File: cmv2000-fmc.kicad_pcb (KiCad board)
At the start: 4 copper layers, 70 x 35 mm, 5 parts, among them P1 FMC_LPC, P2 CONN_31, P3 CONN_51, P4 CONN_2

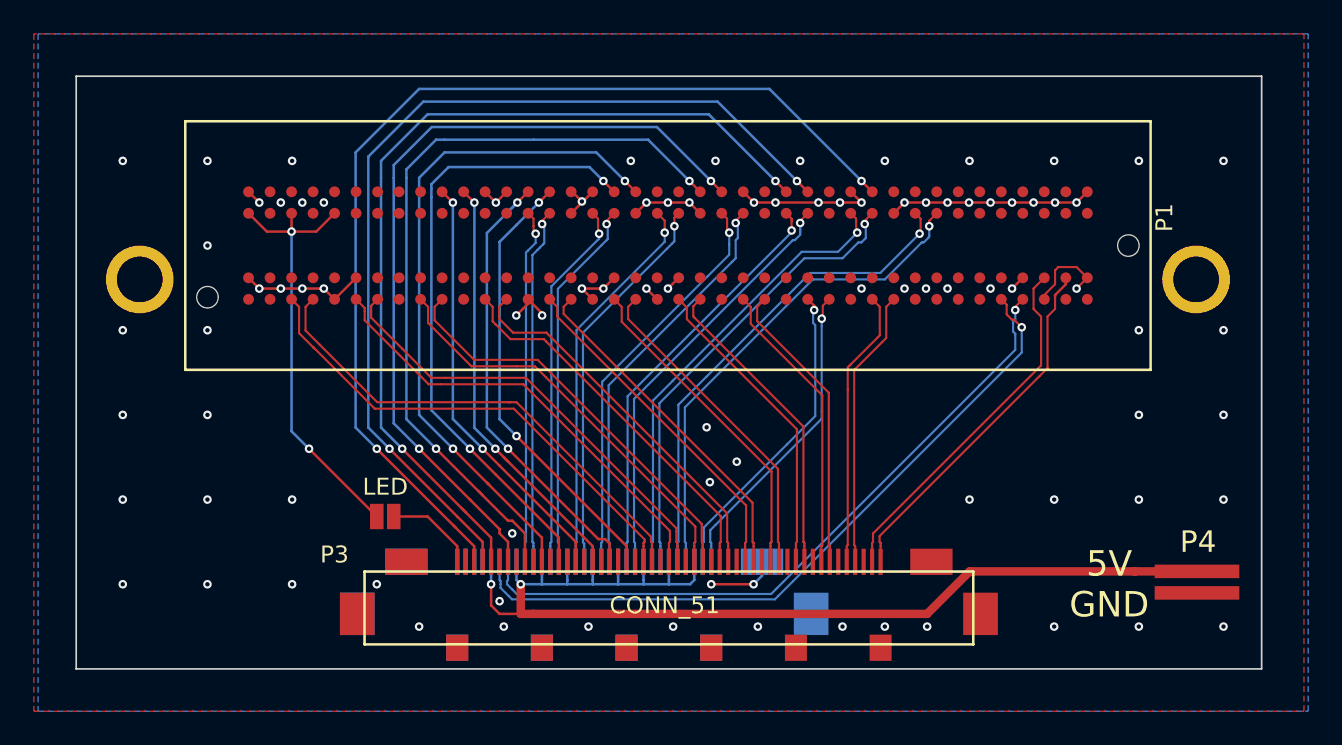
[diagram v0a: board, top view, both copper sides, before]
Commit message: fix mirrored JAE connectors (P2 and P3), correct signal names
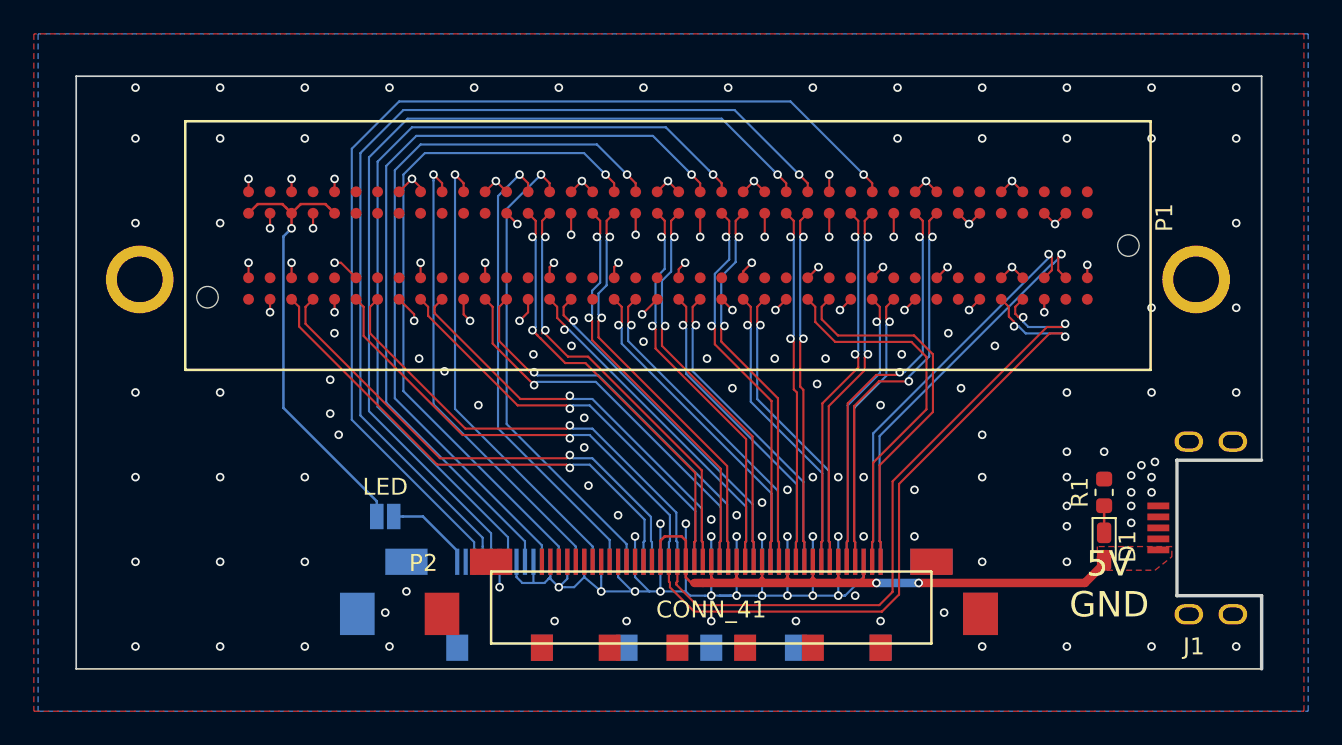
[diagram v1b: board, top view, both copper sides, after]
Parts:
- removed P4: CONN_2, owncomp:FLATCONN_2
- added D1: LED, LED_SMD:LED_0603_1608Metric_Castellated, F.Cu at (173.2, 112.8)
- added J1: USB_B_Micro, owncomp:JAE-USB-DX4R005JJ7, F.Cu at (182.5, 111.7)
- added R1: R, Resistor_SMD:R_0603_1608Metric, F.Cu at (173.2, 109.6)
- JP1, P3: moved to B.Cu
- P2: value CONN_31 -> CONN_41; footprint owncomp:FI-RE31S-HF-R1500 -> owncomp:FI-RE41S-HF-R1500; moved to F.Cu
- moved P2 7.50 mm to (150.0, 114.2), turned to 0 degrees
- turned P3 to 180 degrees
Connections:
- P1 pad C02: Net-(P1-PadC02) -> (no net)
- P1 pad C03: Net-(P1-PadC03) -> (no net)
- P1 pad C06: Net-(P1-PadC06) -> (no net)
- P1 pad C07: Net-(P1-PadC07) -> (no net)
- P1 pad C10: Net-(P1-PadC10) -> (no net)
- P1 pad C11: /SYS_RES_N -> /SDA
- P1 pad C14: /SPI_EN -> /SCL
- P1 pad C15: /SPI_CLK -> /SYS_RES_N
- P1 pad C18: /T_EXP1 -> /SPI_CLK
- P1 pad C19: /SPI_OUT -> /SPI_EN
- P1 pad C22: /SPI_IN -> /SPI_OUT
- P1 pad C23: /T_EXP2 -> /SPI_IN
- P1 pad C30: /SCL -> /T_EXP2
- P1 pad C31: /SDA -> /T_EXP1
- P1 pad C34: Net-(P1-PadC34) -> (no net)
- P1 pad C35: Net-(P1-PadC35) -> (no net)
- P1 pad C37: Net-(P1-PadC37) -> (no net)
- P1 pad C39: Net-(P1-PadC39) -> (no net)
- P1 pad D01: Net-(P1-PadD01) -> (no net)
- P1 pad D04: Net-(P1-PadD04) -> (no net)
- P1 pad D05: Net-(P1-PadD05) -> (no net)
- P1 pad D08: /LVDS_CTR_P -> /LVDS_16_P
- P1 pad D09: /LVDS_CTR_N -> /LVDS_16_N
- P1 pad D11: /LVDS_2_P -> /LVDS_14_P
- P1 pad D12: /LVDS_2_N -> /LVDS_14_N
- P1 pad D14: /LVDS_4_P -> /LVDS_12_P
- P1 pad D15: /LVDS_4_N -> /LVDS_12_N
- P1 pad D17: /LVDS_5_P -> /LVDS_11_P
- P1 pad D18: /LVDS_5_N -> /LVDS_11_N
- P1 pad D20: /LVDS_7_P -> /LVDS_6_P
- P1 pad D21: /LVDS_7_N -> /LVDS_6_N
- P1 pad D23: /LVDS_11_P -> /LVDS_5_P
- P1 pad D24: /LVDS_11_N -> /LVDS_5_N
- P1 pad D26: /LVDS_13_P -> /LVDS_1_P
- P1 pad D27: /LVDS_13_N -> /LVDS_1_N
- P1 pad D29: Net-(P1-PadD29) -> (no net)
- P1 pad D30: Net-(P1-PadD30) -> (no net)
- P1 pad D31: Net-(P1-PadD31) -> (no net)
- P1 pad D32: Net-(P1-PadD32) -> (no net)
- P1 pad D33: Net-(P1-PadD33) -> (no net)
- P1 pad D34: Net-(P1-PadD34) -> (no net)
- P1 pad D35: Net-(P1-PadD35) -> (no net)
- P1 pad G06: Net-(P1-PadG06) -> (no net)
- P1 pad G07: Net-(P1-PadG07) -> (no net)
- P1 pad G09: Net-(P1-PadG09) -> (no net)
- P1 pad G10: Net-(P1-PadG10) -> (no net)
- P1 pad G12: Net-(P1-PadG12) -> (no net)
- P1 pad G13: Net-(P1-PadG13) -> (no net)
- P1 pad G15: Net-(P1-PadG15) -> (no net)
- P1 pad G16: Net-(P1-PadG16) -> (no net)
- P1 pad G18: Net-(P1-PadG18) -> (no net)
- P1 pad G19: Net-(P1-PadG19) -> (no net)
- P1 pad G21: Net-(P1-PadG21) -> (no net)
- P1 pad G22: Net-(P1-PadG22) -> (no net)
- P1 pad G24: Net-(P1-PadG24) -> (no net)
- P1 pad G25: Net-(P1-PadG25) -> (no net)
- P1 pad G27: Net-(P1-PadG27) -> (no net)
- P1 pad G28: Net-(P1-PadG28) -> (no net)
- P1 pad G30: Net-(P1-PadG30) -> (no net)
- P1 pad G31: Net-(P1-PadG31) -> (no net)
- P1 pad G33: Net-(P1-PadG33) -> (no net)
- P1 pad G34: Net-(P1-PadG34) -> (no net)
- P1 pad G36: Net-(P1-PadG36) -> (no net)
- P1 pad G37: Net-(P1-PadG37) -> (no net)
- P1 pad G39: Net-(P1-PadG39) -> (no net)
- P1 pad H01: Net-(P1-PadH01) -> (no net)
- P1 pad H02: Net-(P1-PadH02) -> (no net)
- P1 pad H07: Net-(P1-PadH07) -> (no net)
- P1 pad H08: Net-(P1-PadH08) -> (no net)
- P1 pad H10: /LVDS_1_P -> /LVDS_13_P
- P1 pad H11: /LVDS_1_N -> /LVDS_13_N
- P1 pad H13: /LVDS_3_P -> /LVDS_15_P
- P1 pad H14: /LVDS_3_N -> /LVDS_15_N
- P1 pad H16: /LVDS_6_P -> /LVDS_10_P
- P1 pad H17: /LVDS_6_N -> /LVDS_10_N
- P1 pad H19: /LVDS_8_P -> /LVDS_7_P
- P1 pad H20: /LVDS_8_N -> /LVDS_7_N
- P1 pad H25: /LVDS_10_P -> /LVDS_8_P
- P1 pad H26: /LVDS_10_N -> /LVDS_8_N
- P1 pad H28: /LVDS_12_P -> /LVDS_3_P
- P1 pad H29: /LVDS_12_N -> /LVDS_3_N
- P1 pad H31: /LVDS_14_P -> /LVDS_4_P
- P1 pad H32: /LVDS_14_N -> /LVDS_4_N
- P1 pad H34: /LVDS_15_P -> /LVDS_2_P
- P1 pad H35: /LVDS_15_N -> /LVDS_2_N
- P1 pad H37: /LVDS_16_P -> /LVDS_CTR_P
- P1 pad H38: /LVDS_16_N -> /LVDS_CTR_N
- P1 pad H40: Net-(P1-PadH40) -> (no net)
- P2 pad 1: /LVDS_3_P -> (no net)
- P2 pad 10: /LVDS_4_P -> (no net)
- P2 pad 11: /LVDS_4_N -> (no net)
- P2 pad 12: /5V -> (no net)
- P2 pad 13: /LVDS_5_P -> (no net)
- P2 pad 14: /LVDS_5_N -> (no net)
- P2 pad 16: /LVDS_7_P -> /LVDS_CLK_IN_N
- P2 pad 17: /LVDS_7_N -> /LVDS_CLK_IN_P
- P2 pad 19: /LVDS_11_P -> /LVDS_1_N
- P2 pad 2: /LVDS_3_N -> (no net)
- P2 pad 20: /LVDS_11_N -> /LVDS_1_P
- P2 pad 22: /LVDS_13_P -> /LVDS_5_N
- P2 pad 23: /LVDS_13_N -> /LVDS_5_P
- P2 pad 25: /LVDS_CLK_IN_P -> /LVDS_6_N
- P2 pad 26: /LVDS_CLK_IN_N -> /LVDS_6_P
- P2 pad 28: Net-(P2-Pad28) -> /LVDS_11_N
- P2 pad 29: Net-(P2-Pad29) -> /LVDS_11_P
- P2 pad 3: /5V -> (no net)
- P2 pad 30: Net-(P2-Pad30) -> /5V
- P2 pad 31: Net-(P2-Pad31) -> /LVDS_12_N
- P2 pad 32: GND -> /LVDS_12_P
- P2 pad 33: GND -> /5V
- P2 pad 34: GND -> /LVDS_14_N
- P2 pad 35: GND -> /LVDS_14_P
- P2 pad 36: GND -> /5V
- P2 pad 37: GND -> /LVDS_16_N
- P2 pad 38: GND -> /LVDS_16_P
- P2 pad 39: GND -> /5V
- P2 pad 4: /LVDS_CTR_P -> (no net)
- P2 pad 5: /LVDS_CTR_N -> (no net)
- P2 pad 6: /5V -> (no net)
- P2 pad 7: /LVDS_2_P -> (no net)
- P2 pad 8: /LVDS_2_N -> (no net)
- P2 pad 9: /5V -> (no net)
- P3 pad 1: /LED -> /LVDS_CLK_OUT_P
- P3 pad 10: GND -> /LVDS_7_P
- P3 pad 11: /SPI_IN -> /LVDS_7_N
- P3 pad 13: /T_EXP2 -> /LVDS_9_P
- P3 pad 14: GND -> /LVDS_9_N
- P3 pad 15: /SDA -> GND
- P3 pad 16: GND -> /LVDS_8_P
- P3 pad 17: /SCL -> /LVDS_8_N
- P3 pad 19: /FRAME_REQ -> /LVDS_3_P
- P3 pad 2: /A0 -> /LVDS_CLK_OUT_N
- P3 pad 20: GND -> /LVDS_3_N
- P3 pad 21: /CLK_IN -> GND
- P3 pad 22: GND -> /LVDS_4_P
- P3 pad 23: /LVDS_16_N -> /LVDS_4_N
- P3 pad 24: /LVDS_16_P -> GND
- P3 pad 25: GND -> /LVDS_2_P
- P3 pad 26: /LVDS_15_N -> /LVDS_2_N
- P3 pad 27: /LVDS_15_P -> GND
- P3 pad 28: GND -> /LVDS_CTR_P
- P3 pad 29: /LVDS_14_N -> /LVDS_CTR_N
- P3 pad 3: /SYS_RES_N -> GND
- P3 pad 30: /LVDS_14_P -> GND
- P3 pad 31: GND -> /CLK_IN
- P3 pad 32: /LVDS_12_N -> GND
- P3 pad 33: /LVDS_12_P -> /FRAME_REQ
- P3 pad 35: /LVDS_10_N -> /T_EXP2
- P3 pad 36: /LVDS_10_P -> GND
- P3 pad 37: GND -> /T_EXP1
- P3 pad 38: /LVDS_9_N -> GND
- P3 pad 39: /LVDS_9_P -> /SPI_IN
- P3 pad 4: /SPI_EN -> /LVDS_13_P
- P3 pad 41: /LVDS_8_N -> /SPI_OUT
- P3 pad 42: /LVDS_8_P -> GND
- P3 pad 43: GND -> /SPI_EN
- P3 pad 44: /LVDS_6_N -> GND
- P3 pad 45: /LVDS_6_P -> /SPI_CLK
- P3 pad 47: /LVDS_1_N -> /SYS_RES_N
- P3 pad 48: /LVDS_1_P -> /SCL
- P3 pad 49: GND -> /SDA
- P3 pad 5: /SPI_CLK -> /LVDS_13_N
- P3 pad 50: /LVDS_CLK_OUT_N -> (no net)
- P3 pad 51: /LVDS_CLK_OUT_P -> /LED
- P3 pad 7: /T_EXP1 -> /LVDS_10_P
- P3 pad 8: GND -> /LVDS_10_N
- P3 pad 9: /SPI_OUT -> GND
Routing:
- net GND: track 332.5 -> 125.7 mm, vias 89 -> 173
- net /SDA: track 25.1 -> 61.8 mm, vias 2 -> 1
- net /SCL: track 25.4 -> 56.9 mm, vias 2 -> 1
- net /T_EXP1: track 48.2 -> 27.6 mm, vias 2 -> 1
- net /5V: track 68.1 -> 48.1 mm
- net /T_EXP2: track 37.2 -> 27.5 mm, vias 2 -> 1
- net /LVDS_1_P: track 16.5 -> 25.8 mm, vias 0 -> 2
- net /LVDS_1_N: track 16.7 -> 26.0 mm, vias 0 -> 2
- net /SPI_EN: track 56.2 -> 47.7 mm, vias 2 -> 1
- net /SYS_RES_N: track 61.8 -> 54.5 mm, vias 2 -> 1
- net /LVDS_6_N: track 17.5 -> 23.5 mm, vias 0 -> 2
- net /LVDS_6_P: track 17.5 -> 23.5 mm, vias 0 -> 2
- net /LVDS_16_N: track 29.1 -> 23.7 mm, vias 0 -> 2
- net /LVDS_16_P: track 29.2 -> 23.8 mm, vias 0 -> 2
- net /LVDS_3_P: track 18.7 -> 23.5 mm
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- added copper zone on F.Cu, net /5V
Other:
- outline, holes or cut-outs redrawn
- board text added: "CMV2000 to FMC v0.2 2018-12-03"
- board text removed: "CMV2000 to FMC v0.1 2014-12-09"

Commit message: first version of layout (still WIP)
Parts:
- added C1: 10uF, 25V, Capacitor_SMD:C_1206_3216Metric, B.Cu at (180.7, 111.2)
- added C10: TBD, Capacitor_SMD:C_0805_2012Metric, B.Cu at (166.5, 112.1)
- added C2: 100n, Capacitor_SMD:C_0402_1005Metric, B.Cu at (128.2, 96.2)
- added C3: 10n, Capacitor_SMD:C_0402_1005Metric, B.Cu at (177.5, 113.8)
- added C4: 22uF, 10V, Capacitor_SMD:C_1206_3216Metric, B.Cu at (174.1, 113.8)
- added C5: 100n, Capacitor_SMD:C_0402_1005Metric, B.Cu at (128.2, 92.0)
- added C6: 1u, Capacitor_SMD:C_0603_1608Metric, B.Cu at (179.0, 93.0)
- added C7: 100n, Capacitor_SMD:C_0402_1005Metric, B.Cu at (114.4, 89.4)
- added C8: 1n, Capacitor_SMD:C_0402_1005Metric, B.Cu at (178.6, 88.4)
- added C9: 100n, Capacitor_SMD:C_0402_1005Metric, B.Cu at (116.4, 94.0)
- added D2: LED, footprints:150060VS75000, B.Cu at (116.0, 87.0)
- added D3: LED, footprints:150060VS75000, B.Cu at (122.1, 115.3)
- added J10: LVDS_CTR_P, footprints:U.FL-R-SMT-1, B.Cu at (130.8, 106.6)
- added J11: LVDS_CTR_N, footprints:U.FL-R-SMT-1, B.Cu at (135.3, 106.6)
- added J12: LVDS_1_P, footprints:U.FL-R-SMT-1, B.Cu at (142.9, 92.0)
- added J13: LVDS_1_N, footprints:U.FL-R-SMT-1, B.Cu at (137.8, 92.0)
- added J14: LVDS_2_P, footprints:U.FL-R-SMT-1, B.Cu at (136.9, 97.3)
- added J15: LVDS_2_N, footprints:U.FL-R-SMT-1, B.Cu at (132.6, 97.4)
- added J2: Conn_02x05, footprints:TSM-105-01-L-DV, B.Cu at (120.8, 107.0)
- added J3: LVDS_CLK_IN_P, footprints:U.FL-R-SMT-1, B.Cu at (164.1, 102.8)
- added J4: LVDS_CLK_IN_N, footprints:U.FL-R-SMT-1, B.Cu at (172.1, 102.8)
- added J5: LVDS_CLK_OUT_P, footprints:U.FL-R-SMT-1, B.Cu at (172.6, 92.2)
- added J6: LVDS_CLK_OUT_N, footprints:U.FL-R-SMT-1, B.Cu at (168.1, 92.2)
- added J7: CLK_IN, footprints:U.FL-R-SMT-1, B.Cu at (130.4, 101.2)
- added J8: CLK_IN, footprints:U.FL-R-SMT-1, B.Cu at (145.4, 88.0)
- added J9: Conn_01x02, footprints:TSM-102-01-L-SV, B.Cu at (117.1, 116.2)
- added L1: 4.7uH, footprints:NRS4018, B.Cu at (177.5, 116.5)
- added Q1: Q_NMOS_GSD, Package_TO_SOT_SMD:SOT-323_SC-70, B.Cu at (132.4, 94.2)
- added R10: 9.53k, Resistor_SMD:R_0402_1005Metric, B.Cu at (175.0, 107.7)
- added R11: 0, Resistor_SMD:R_0402_1005Metric, B.Cu at (162.5, 89.6)
- added R12: 0, Resistor_SMD:R_0402_1005Metric, B.Cu at (135.5, 94.5)
- added R13: 0, Resistor_SMD:R_1206_3216Metric, B.Cu at (172.9, 117.3)
- added R14: 0, Resistor_SMD:R_0402_1005Metric, B.Cu at (171.5, 97.7)
- added R15: 1k, Resistor_SMD:R_0402_1005Metric, B.Cu at (167.2, 102.8)
- added R16: 1k, Resistor_SMD:R_0402_1005Metric, B.Cu at (169.0, 102.8)
- added R17: DNP, Resistor_SMD:R_0402_1005Metric, B.Cu at (166.1, 97.4)
- added R18: 0, Resistor_SMD:R_0402_1005Metric, B.Cu at (162.5, 88.6)
- added R19: 270R, Resistor_SMD:R_0603_1608Metric, B.Cu at (114.1, 92.9)
- added R2: DNP, Resistor_SMD:R_0402_1005Metric, B.Cu at (113.9, 100.1)
- added R20: DNP, Resistor_SMD:R_0402_1005Metric, B.Cu at (166.1, 98.4)
- added R21: 620R, Resistor_SMD:R_0603_1608Metric, B.Cu at (125.2, 116.2)
- added R22: TBD, Resistor_SMD:R_0603_1608Metric, B.Cu at (125.2, 117.8)
- added R23: 1k, Resistor_SMD:R_0402_1005Metric, B.Cu at (170.8, 94.4)
- added R24: 1k, Resistor_SMD:R_0402_1005Metric, B.Cu at (169.9, 94.4)
- added R25: 1k, Resistor_SMD:R_0402_1005Metric, B.Cu at (127.9, 102.5)
- added R26: 1k, Resistor_SMD:R_0402_1005Metric, B.Cu at (142.3, 88.0)
- added R27: 100k, Resistor_SMD:R_0402_1005Metric, B.Cu at (178.6, 87.3)
- added R28: 1k, Resistor_SMD:R_0402_1005Metric, B.Cu at (175.1, 87.0)
- added R29: 1M, Resistor_SMD:R_0402_1005Metric, B.Cu at (118.1, 92.5)
- added R3: DNP, Resistor_SMD:R_0402_1005Metric, B.Cu at (115.0, 100.6)
- added R30: 1k, Resistor_SMD:R_0402_1005Metric, B.Cu at (131.8, 104.0)
- added R31: 1k, Resistor_SMD:R_0402_1005Metric, B.Cu at (134.0, 104.0)
- added R32: 1k, Resistor_SMD:R_0402_1005Metric, B.Cu at (141.9, 94.8)
- added R33: 1k, Resistor_SMD:R_0402_1005Metric, B.Cu at (139.0, 94.8)
- added R34: 1k, Resistor_SMD:R_0402_1005Metric, B.Cu at (135.5, 99.8)
- added R35: 1k, Resistor_SMD:R_0402_1005Metric, B.Cu at (134.1, 99.8)
- added R36: DNP, Resistor_SMD:R_0402_1005Metric, B.Cu at (126.5, 114.5)
- added R4: 10k, Resistor_SMD:R_0402_1005Metric, B.Cu at (118.9, 99.6)
- added R5: 10k, Resistor_SMD:R_0402_1005Metric, B.Cu at (177.7, 107.7)
- added R6: 10k, Resistor_SMD:R_0402_1005Metric, B.Cu at (129.3, 94.6)
- added R7: 10k, Resistor_SMD:R_0402_1005Metric, B.Cu at (126.7, 98.3)
- added R8: 10k, Resistor_SMD:R_0402_1005Metric, B.Cu at (121.3, 99.6)
- added R9: 49.9k, Resistor_SMD:R_0402_1005Metric, B.Cu at (172.9, 107.7)
- added RN1: R_NET_BUS_8, 1M, footprints:EXB-A10P, B.Cu at (131.8, 89.0)
- added U1: AP3211, Package_TO_SOT_SMD:SOT-23-6, B.Cu at (177.4, 111.5)
- added U2: SN74AXC8T245, Package_SO:TSSOP-24_4.4x7.8mm_P0.65mm, B.Cu at (123.4, 93.5)
- added U3: BD49xxx_GND1, footprints:SSOP3, B.Cu at (178.5, 90.8)
- added U4: SN74LVC2T45, Package_SO:VSSOP-8_2.4x2.1mm_P0.5mm, B.Cu at (116.2, 91.2)
- D1: value LED -> D; footprint LED_SMD:LED_0603_1608Metric_Castellated -> footprints:NRVTS245ESF; moved to B.Cu
- J1: value USB_B_Micro -> Conn_01x02; footprint owncomp:JAE-USB-DX4R005JJ7 -> footprints:TSM-102-01-L-SV; moved to B.Cu
- R1: value R -> DNP; footprint Resistor_SMD:R_0603_1608Metric -> Resistor_SMD:R_0402_1005Metric; moved to B.Cu
- moved R1 26.7 mm to (155.7, 89.4)
- moved J1 12.4 mm to (170.2, 112.9), turned to 0 degrees
- moved JP1 10.5 mm to (122.4, 117.4), turned to 90 degrees
- moved D1 8.72 mm to (181.0, 116.7), turned to 90 degrees
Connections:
- D1 pad 1: Net-(D1-Pad1) -> Net-(C3-Pad2)
- D1 pad 2: /5V -> GND
- J1 pad 1: /5V -> /5V_CAM
- J1 pad 2: (no net) -> GND
- JP1 pad 1: /LED -> Net-(JP1-Pad1)
- JP1 pad 2: /3.3V -> /LED
- P1 pad C02: (no net) -> Net-(P1-PadC02)
- P1 pad C03: (no net) -> Net-(P1-PadC03)
- P1 pad C06: (no net) -> Net-(P1-PadC06)
- P1 pad C07: (no net) -> Net-(P1-PadC07)
- P1 pad C10: (no net) -> /T_EXP1_FMC
- P1 pad C11: /SDA -> /T_EXP2_FMC
- P1 pad C14: /SCL -> Net-(P1-PadC14)
- P1 pad C15: /SYS_RES_N -> /SYS_RES_N_FMC
- P1 pad C18: /SPI_CLK -> /SPI_CLK_FMC
- P1 pad C19: /SPI_EN -> /SPI_EN_FMC
- P1 pad C22: /SPI_OUT -> /SPI_OUT_FMC
- P1 pad C23: /SPI_IN -> /SPI_IN_FMC
- P1 pad C26: /CLK_IN -> /CLK_IN_FMC
- P1 pad C27: /FRAME_REQ -> /FRAME_REQ_FMC
- P1 pad C30: /T_EXP2 -> Net-(P1-PadC30)
- P1 pad C31: /T_EXP1 -> Net-(P1-PadC31)
- P1 pad C34: (no net) -> Net-(P1-PadC34)
- P1 pad C35: (no net) -> +12V
- P1 pad C37: (no net) -> +12V
- P1 pad C39: (no net) -> Net-(P1-PadC39)
- P1 pad D01: (no net) -> Net-(P1-PadD01)
- P1 pad D04: (no net) -> Net-(P1-PadD04)
- P1 pad D05: (no net) -> Net-(P1-PadD05)
- P1 pad D29: (no net) -> Net-(P1-PadD29)
- P1 pad D30: (no net) -> Net-(P1-PadD30)
- P1 pad D31: (no net) -> Net-(P1-PadD31)
- P1 pad D32: (no net) -> Net-(P1-PadD32)
- P1 pad D33: (no net) -> Net-(P1-PadD33)
- P1 pad D34: (no net) -> Net-(P1-PadD34)
- P1 pad D35: (no net) -> Net-(P1-PadD35)
- P1 pad D36: /3.3V -> +3V3
- P1 pad D38: /3.3V -> +3V3
- P1 pad D40: /3.3V -> +3V3
- P1 pad G06: (no net) -> Net-(P1-PadG06)
- P1 pad G07: (no net) -> Net-(P1-PadG07)
- P1 pad G09: (no net) -> Net-(P1-PadG09)
- P1 pad G10: (no net) -> Net-(P1-PadG10)
- P1 pad G12: (no net) -> Net-(P1-PadG12)
- P1 pad G13: (no net) -> Net-(P1-PadG13)
- P1 pad G15: (no net) -> Net-(P1-PadG15)
- P1 pad G16: (no net) -> Net-(P1-PadG16)
- P1 pad G18: (no net) -> Net-(P1-PadG18)
- P1 pad G19: (no net) -> Net-(P1-PadG19)
- P1 pad G21: (no net) -> Net-(P1-PadG21)
- P1 pad G22: (no net) -> Net-(P1-PadG22)
- P1 pad G24: (no net) -> Net-(P1-PadG24)
- P1 pad G25: (no net) -> Net-(P1-PadG25)
- P1 pad G27: (no net) -> Net-(P1-PadG27)
- P1 pad G28: (no net) -> Net-(P1-PadG28)
- P1 pad G30: (no net) -> Net-(P1-PadG30)
- P1 pad G31: (no net) -> Net-(P1-PadG31)
- P1 pad G33: (no net) -> Net-(P1-PadG33)
- P1 pad G34: (no net) -> Net-(P1-PadG34)
- P1 pad G36: (no net) -> Net-(P1-PadG36)
- P1 pad G37: (no net) -> Net-(P1-PadG37)
- P1 pad G39: (no net) -> /VIO_FMC
- P1 pad H01: (no net) -> Net-(P1-PadH01)
- P1 pad H02: (no net) -> Net-(P1-PadH02)
- P1 pad H04: /LVDS_CLK_IN_P -> Net-(P1-PadH04)
- P1 pad H05: /LVDS_CLK_IN_N -> Net-(P1-PadH05)
- P1 pad H07: (no net) -> Net-(P1-PadH07)
- P1 pad H08: (no net) -> Net-(P1-PadH08)
- P1 pad H40: (no net) -> Net-(P1-PadH40)
- P2 pad 1: (no net) -> Net-(P2-Pad1)
- P2 pad 10: (no net) -> Net-(P2-Pad10)
- P2 pad 11: (no net) -> Net-(P2-Pad11)
- P2 pad 12: (no net) -> Net-(P2-Pad12)
- P2 pad 13: (no net) -> Net-(P2-Pad13)
- P2 pad 14: (no net) -> Net-(P2-Pad14)
- P2 pad 15: /5V -> /5V_CAM
- P2 pad 18: /5V -> /5V_CAM
- P2 pad 2: (no net) -> Net-(P2-Pad2)
- P2 pad 21: /5V -> /5V_CAM
- P2 pad 24: /5V -> /5V_CAM
- P2 pad 27: /5V -> /5V_CAM
- P2 pad 3: (no net) -> Net-(P2-Pad3)
- P2 pad 30: /5V -> /5V_CAM
- P2 pad 33: /5V -> /5V_CAM
- P2 pad 36: /5V -> /5V_CAM
- P2 pad 39: /5V -> /5V_CAM
- P2 pad 4: (no net) -> Net-(P2-Pad4)
- P2 pad 5: (no net) -> Net-(P2-Pad5)
- P2 pad 6: (no net) -> Net-(P2-Pad6)
- P2 pad 7: (no net) -> Net-(P2-Pad7)
- P2 pad 8: (no net) -> Net-(P2-Pad8)
- P2 pad 9: (no net) -> Net-(P2-Pad9)
- P3 pad 50: (no net) -> /A0
- R1 pad 1: Net-(D1-Pad1) -> Net-(P1-PadC14)
- R1 pad 2: GND -> /CAM_PWR_ON
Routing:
- net /5V_CAM: track 0.00 -> 127.9 mm, vias 0 -> 4
- net +12V: track 0.00 -> 94.2 mm, vias 0 -> 2
- net /CAM_PWR_GOOD: track 0.00 -> 81.4 mm, vias 0 -> 4
- net GND: track 125.7 -> 199.3 mm, vias 173 -> 138
- net /CAM_PWR_GOOD_FMC: track 0.00 -> 49.0 mm, vias 0 -> 2
- net /5V: track 48.1 -> 0.00 mm, vias 2 -> 0
- net /CAM_PWR_ON: track 0.00 -> 48.1 mm
- net /T_EXP1_FMC: track 0.00 -> 42.7 mm, vias 0 -> 1
- net /T_EXP2_FMC: track 0.00 -> 40.7 mm, vias 0 -> 1
- net /SYS_RES_N_FMC: track 0.00 -> 39.4 mm, vias 0 -> 1
- net Net-(P1-PadH07): track 0.00 -> 35.2 mm, vias 0 -> 1
- net /SPI_CLK_FMC: track 0.00 -> 34.5 mm, vias 0 -> 1
- net /SPI_OUT_FMC: track 0.00 -> 34.1 mm, vias 0 -> 1
- net Net-(P1-PadC31): track 0.00 -> 33.5 mm, vias 0 -> 1
- net /SPI_EN_FMC: track 0.00 -> 31.5 mm, vias 0 -> 1
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- added copper zone on B.Cu, net +12V
- added copper zone on B.Cu, net Net-(C3-Pad2)
- added copper zone on B.Cu, net Net-(C4-Pad1)
- removed copper zone on F.Cu, net /5V
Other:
- outline, holes or cut-outs redrawn
- net class DIFF_PAIR added: clearance 0.1, trace_width 0.1, via_dia 0.508, via_drill 0.3048
- net class Power added: clearance 0.2, trace_width 0.5, via_dia 0.508, via_drill 0.3048
- net class PowerSmall added: clearance 0.15, trace_width 0.3, via_dia 0.508, via_drill 0.3048
- rule trace_min: 0.127 -> 0.1
- board text removed: "5V GND"
- board text removed: "LED"

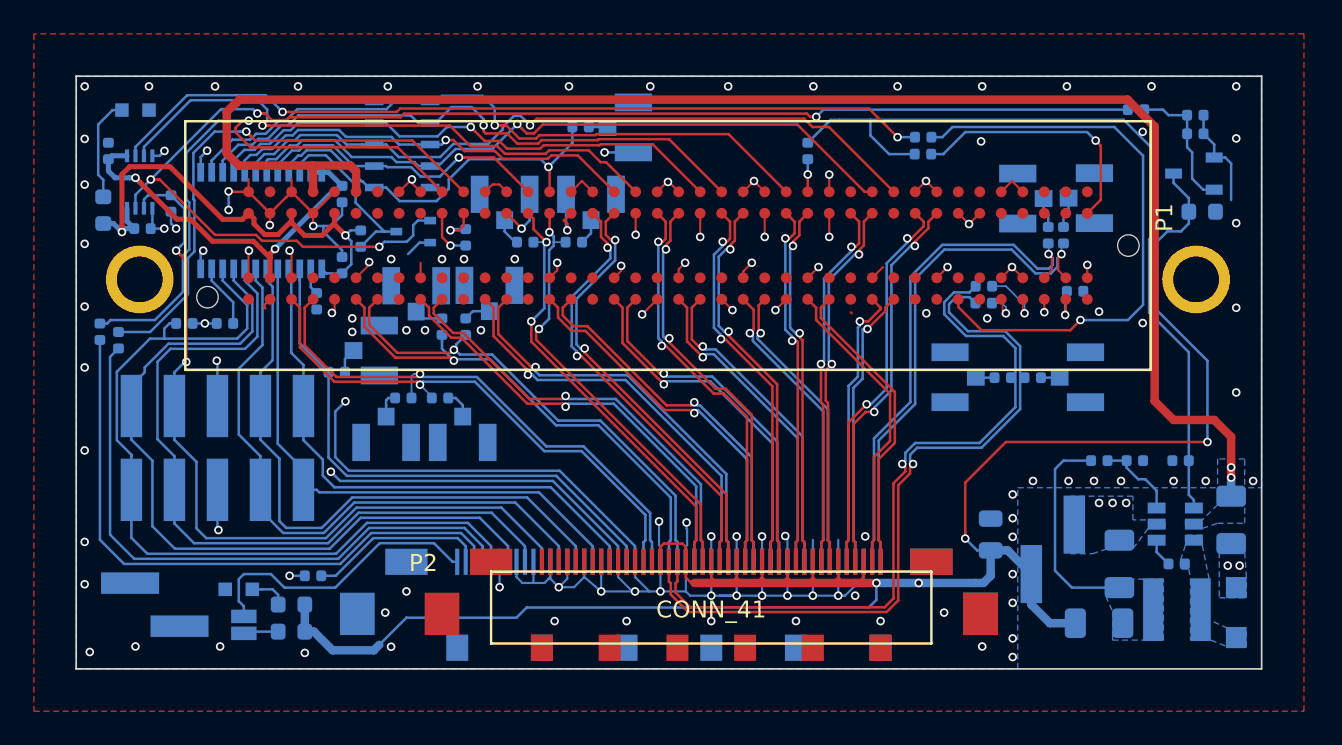
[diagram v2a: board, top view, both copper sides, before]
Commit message: update Samtec FMC ASP-134604-01 connector
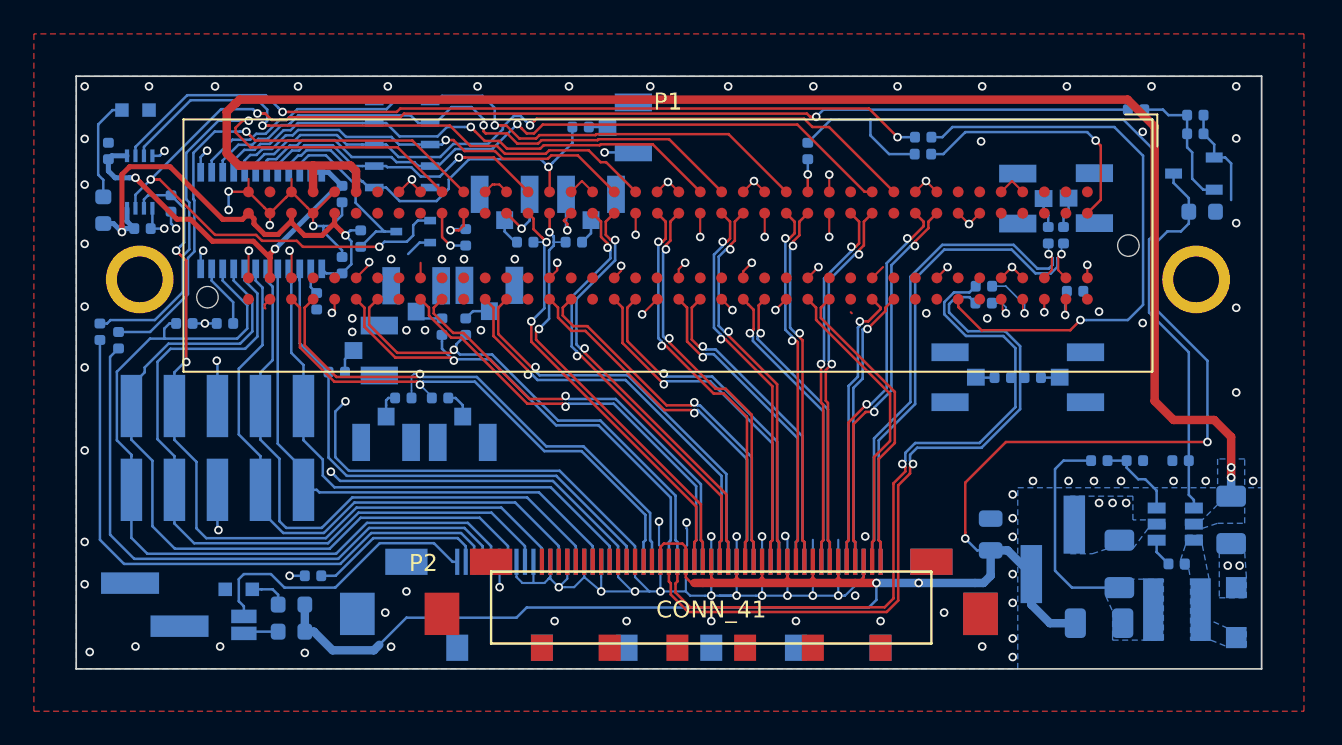
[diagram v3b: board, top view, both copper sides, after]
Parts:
- P1: footprint Connect:FMC_LPC_ASP-134604-01 -> Connector_Samtec:Samtec_FMC_ASP-134604-01_4x40_Vertical
- turned P1 to 270 degrees
